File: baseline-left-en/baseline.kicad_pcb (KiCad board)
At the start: 2 copper layers, 18 parts, among them J1 TYPE-C-31-M-12, SW1 TS-1088-AR02016, SW2 TS-1088-AR02016, U3 LD1117S33TR_SOT223

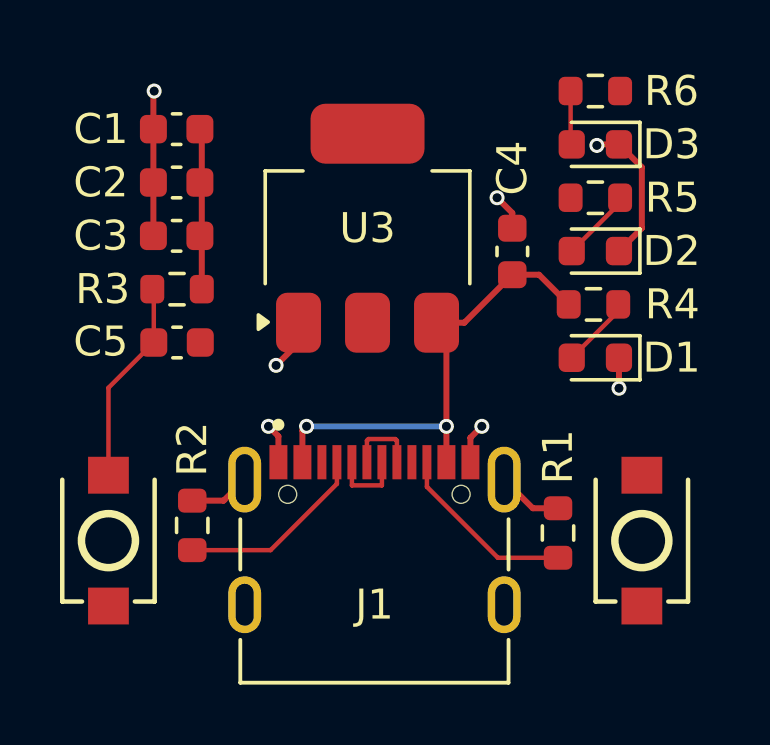
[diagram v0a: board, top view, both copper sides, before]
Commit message: 0.4mm power nets
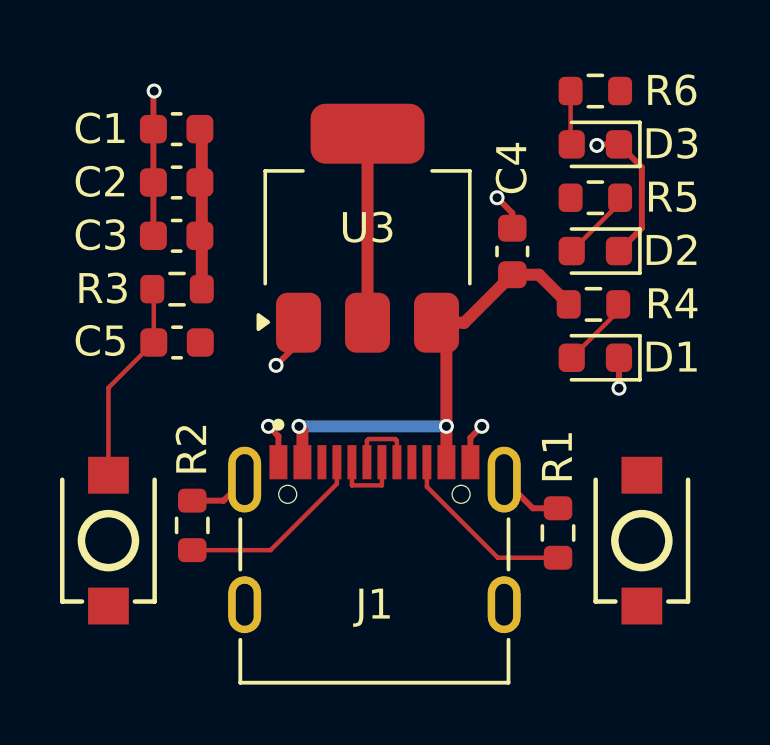
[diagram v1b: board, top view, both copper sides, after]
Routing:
- net +3V3: track 5.58 -> 11.9 mm
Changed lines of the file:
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@@
 		(capping no)
 		(filling no)
+		(zone_defaults)
 		(pcbplotparams
 			(layerselection 0x00000000_00000000_55555555_5755f5ff)
@@
 	)
 	(segment
-		(start 154.241 75.184)
-		(end 154.241 69.913)
+		(start 154.33 70.002)
+		(end 154.178 69.85)
 		(width 0.2)
 		(layer "F.Cu")
@@
 	)
 	(segment
-		(start 154.33 70.002)
+		(start 154.241 69.913)
 		(end 154.178 69.85)
-		(width 0.2)
+		(width 0.4)
 		(layer "F.Cu")
 		(net "+3V3")
 	)
 	(segment
-		(start 154.241 69.913)
-		(end 154.178 69.85)
-		(width 0.2)
+		(start 159.766 76.302)
+		(end 159.766 70.002)
+		(width 0.4)
+		(layer "F.Cu")
+		(net "+3V3")
+	)
+	(segment
+		(start 154.241 75.184)
+		(end 154.241 69.913)
+		(width 0.4)
 		(layer "F.Cu")
 		(net "+3V3")
@@
 	)
 	(segment
-		(start 162.992 76.302)
-		(end 164.592 74.702)
-		(width 0.2)
-		(layer "F.Cu")
-		(net "+5V")
-	)
-	(segment
-		(start 164.592 74.702)
-		(end 165.4825 74.702)
-		(width 0.2)
+		(start 157.5955 79.8715)
+		(end 157.48 79.756)
+		(width 0.4)
 		(layer "F.Cu")
 		(net "+5V")
 	)
 	(segment
-		(start 157.5955 79.8945)
-		(end 157.734 79.756)
-		(width 0.2)
+		(start 157.5955 80.952)
+		(end 157.5955 79.8715)
+		(width 0.4)
 		(layer "F.Cu")
 		(net "+5V")
 	)
 	(segment
-		(start 165.4825 74.702)
-		(end 166.4725 75.692)
-		(width 0.2)
+		(start 162.3955 79.756)
+		(end 162.3955 76.6315)
+		(width 0.4)
 		(layer "F.Cu")
 		(net "+5V")
@@
 		(start 162.3955 80.952)
 		(end 162.3955 79.756)
-		(width 0.2)
+		(width 0.4)
 		(layer "F.Cu")
 		(net "+5V")
 	)
 	(segment
-		(start 162.3955 79.756)
-		(end 162.3955 76.6315)
-		(width 0.2)
+		(start 162.992 76.302)
+		(end 164.592 74.702)
+		(width 0.4)
 		(layer "F.Cu")
 		(net "+5V")
 	)
 	(segment
-		(start 157.5955 80.952)
-		(end 157.5955 79.8945)
-		(width 0.2)
+		(start 162.066 76.302)
+		(end 162.992 76.302)
+		(width 0.4)
 		(layer "F.Cu")
 		(net "+5V")
 	)
 	(segment
-		(start 162.066 76.302)
-		(end 162.992 76.302)
-		(width 0.2)
+		(start 165.4825 74.702)
+		(end 166.4725 75.692)
+		(width 0.4)
 		(layer "F.Cu")
 		(net "+5V")
@@
 		(start 162.3955 76.6315)
 		(end 162.066 76.302)
-		(width 0.2)
+		(width 0.4)
+		(layer "F.Cu")
+		(net "+5V")
+	)
+	(segment
+		(start 164.592 74.702)
+		(end 165.4825 74.702)
+		(width 0.4)
 		(layer "F.Cu")
 		(net "+5V")
 	)
 	(via
-		(at 162.3955 79.756)
+		(at 157.48 79.756)
 		(size 0.5)
 		(drill 0.3)
@@
 	)
 	(via
-		(at 157.734 79.756)
+		(at 162.3955 79.756)
 		(size 0.5)
 		(drill 0.3)
@@
 	)
 	(segment
-		(start 157.734 79.756)
+		(start 157.48 79.756)
 		(end 162.3955 79.756)
-		(width 0.2)
+		(width 0.4)
 		(layer "B.Cu")
 		(net "+5V")
